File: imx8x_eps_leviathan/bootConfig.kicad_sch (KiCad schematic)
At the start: 24 parts, among them SW1 SW_DIP_x01, U18 BD2204GUL-E2

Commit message: Did stufffffff
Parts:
- C58, C59, C60: footprint (none) -> EPS:C0402
- R100, R101, R84, R85, R86, R87, R88, R89, R90, R91, R92, R93, R94, R95, R96, R97, R98, R99: footprint (none) -> EPS:R0402
- SW1: footprint (none) -> imx8_carrier_board_footprints:SW-SMD_1.27-1P-TPPT
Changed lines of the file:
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@@
 			)
 		)
-		(property "Footprint" ""
+		(property "Footprint" "EPS:R0402"
 			(at 157.226 41.656 90)
 			(effects
@@
 			)
 		)
-		(property "Footprint" ""
+		(property "Footprint" "EPS:C0402"
 			(at 201.6252 33.02 0)
 			(effects
@@
 			)
 		)
-		(property "Footprint" ""
+		(property "Footprint" "EPS:R0402"
 			(at 131.064 28.956 90)
 			(effects
@@
 			)
 		)
-		(property "Footprint" ""
+		(property "Footprint" "EPS:C0402"
 			(at 194.6148 33.02 0)
 			(effects
@@
 			)
 		)
-		(property "Footprint" ""
+		(property "Footprint" "EPS:R0402"
 			(at 30.734 70.866 90)
 			(effects
@@
 			)
 		)
-		(property "Footprint" ""
+		(property "Footprint" "EPS:R0402"
 			(at 152.146 28.956 90)
 			(effects
@@
 			)
 		)
-		(property "Footprint" ""
+		(property "Footprint" "EPS:R0402"
 			(at 115.824 28.956 90)
 			(effects
@@
 			)
 		)
-		(property "Footprint" ""
+		(property "Footprint" "EPS:R0402"
 			(at 43.434 70.866 90)
 			(effects
@@
 			)
 		)
-		(property "Footprint" ""
+		(property "Footprint" "imx8_carrier_board_footprints:SW-SMD_1.27-1P-TPPT"
 			(at 31.75 85.09 0)
 			(effects
@@
 			)
 		)
-		(property "Footprint" ""
+		(property "Footprint" "EPS:R0402"
 			(at 157.226 39.116 90)
 			(effects
@@
 			)
 		)
-		(property "Footprint" ""
+		(property "Footprint" "EPS:R0402"
 			(at 201.676 25.146 90)
 			(effects
@@
 			)
 		)
-		(property "Footprint" ""
+		(property "Footprint" "EPS:R0402"
 			(at 30.734 97.536 90)
 			(effects
@@
 			)
 		)
-		(property "Footprint" ""
+		(property "Footprint" "EPS:R0402"
 			(at 146.304 28.956 90)
 			(effects
@@
 			)
 		)
-		(property "Footprint" ""
+		(property "Footprint" "EPS:R0402"
 			(at 123.444 28.956 90)
 			(effects
@@
 			)
 		)
-		(property "Footprint" ""
+		(property "Footprint" "EPS:R0402"
 			(at 157.226 54.356 90)
 			(effects
@@
 			)
 		)
-		(property "Footprint" ""
+		(property "Footprint" "EPS:C0402"
 			(at 35.56 45.4152 0)
 			(effects
@@
 			)
 		)
-		(property "Footprint" ""
+		(property "Footprint" "EPS:R0402"
 			(at 185.674 26.416 90)
 			(effects
@@
 			)
 		)
-		(property "Footprint" ""
+		(property "Footprint" "EPS:R0402"
 			(at 157.226 36.576 90)
 			(effects
@@
 			)
 		)
-		(property "Footprint" ""
+		(property "Footprint" "EPS:R0402"
 			(at 43.434 97.536 90)
 			(effects
@@
 			)
 		)
-		(property "Footprint" ""
+		(property "Footprint" "EPS:R0402"
 			(at 157.226 51.816 90)
 			(effects
@@
 			)
 		)
-		(property "Footprint" ""
+		(property "Footprint" "EPS:R0402"
 			(at 138.684 28.956 90)
 			(effects
@@
 			)
 		)
-		(property "Footprint" ""
+		(property "Footprint" "EPS:R0402"
 			(at 37.084 97.536 90)
 			(effects

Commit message: bruh
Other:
- title: (none) -> Leviathan 1-A
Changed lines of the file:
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@@
 	(paper "A4")
 	(title_block
+		(title "Leviathan 1-A")
+		(date "2025-10-22")
+		(rev "1-A")
 		(company "Bronco Space Lab")
 		(comment 1 "By John Pollak & Luca Lanzillotta")

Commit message: Updated Schematic and SOM
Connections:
- net VCC_3V3_OUT is gone; now on net +3.3V_OBC: C58.2, U18.A1 (VIN1)
- net VCC_3V3 renamed +3.3V_OBC
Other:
- moved on the sheet: C58, U18

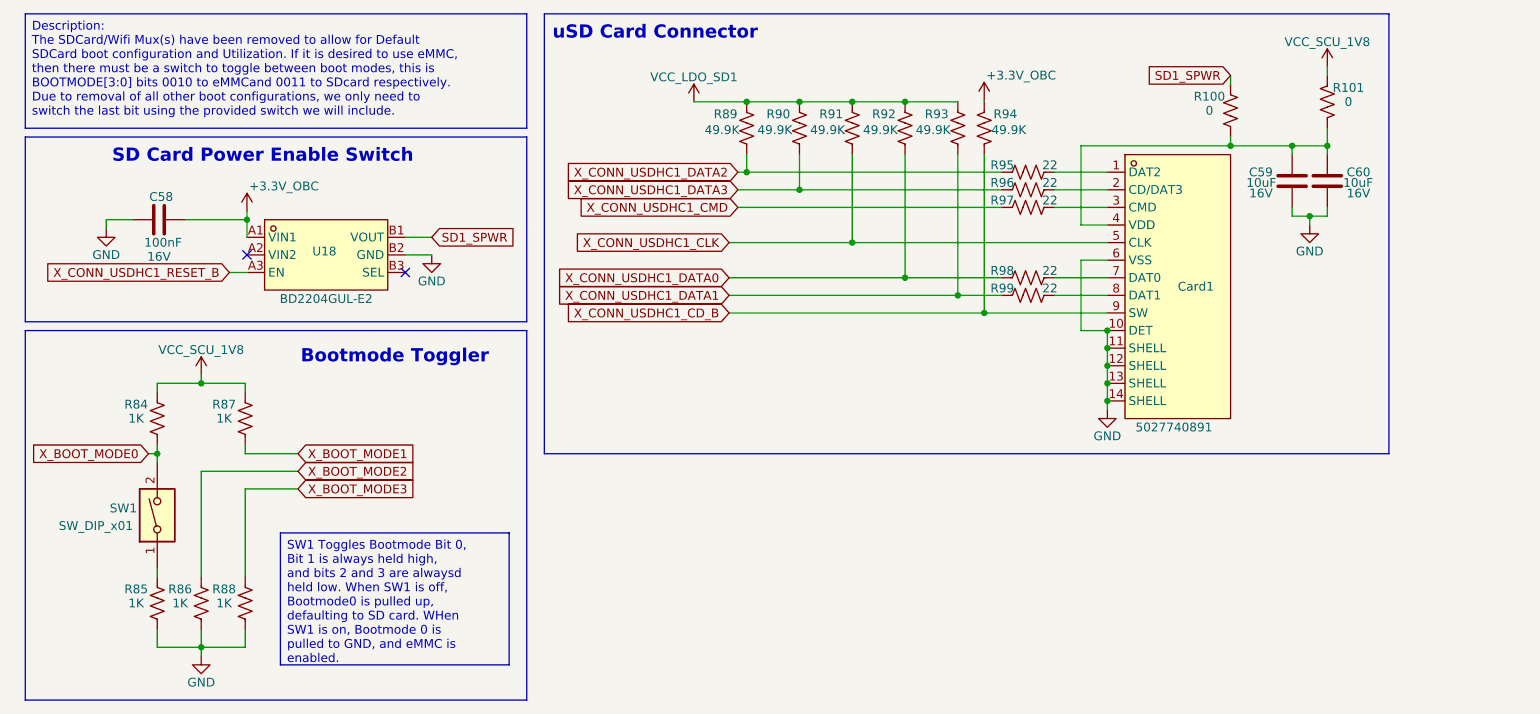
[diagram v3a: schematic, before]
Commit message: Completed Schematic, Started Layout
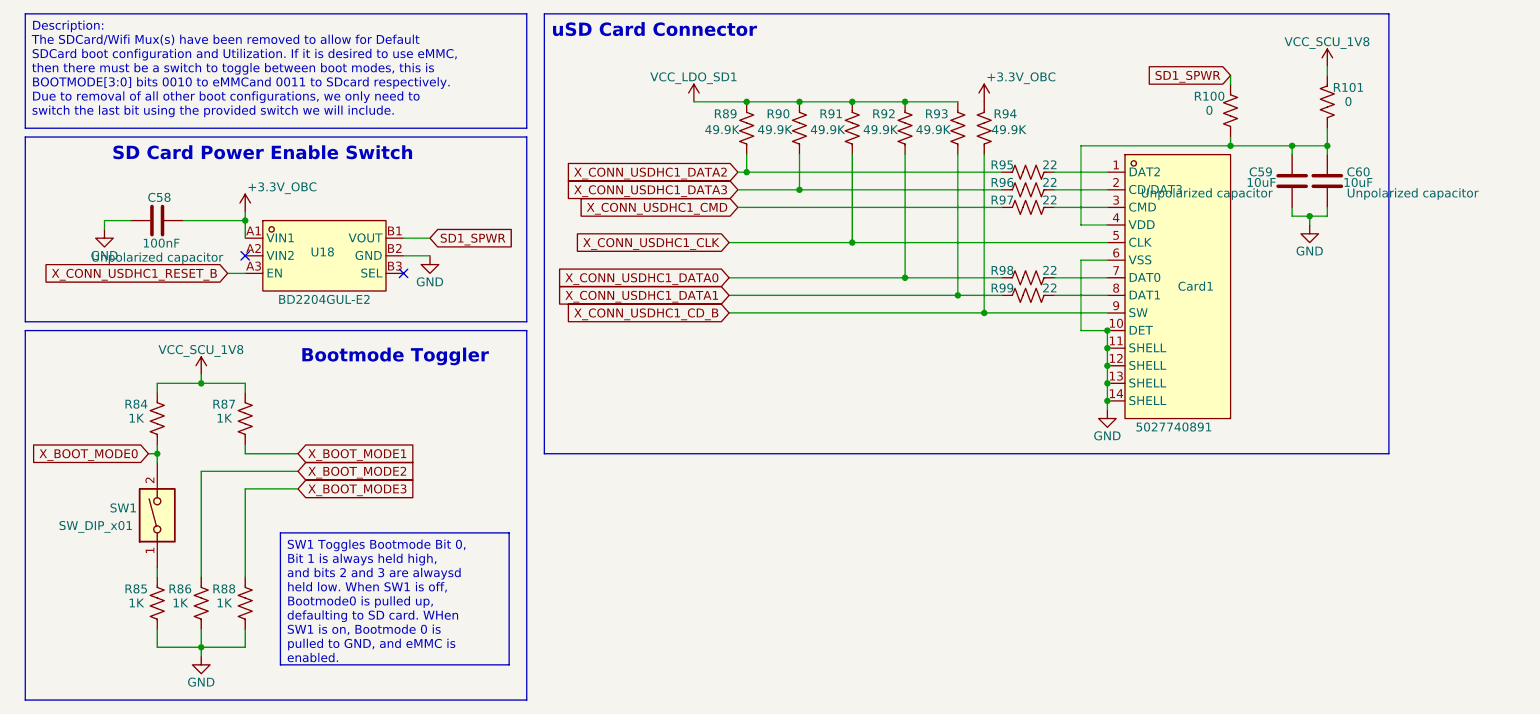
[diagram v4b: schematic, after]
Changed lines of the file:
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@@
 	(title_block
 		(title "Leviathan 1-A")
-		(date "2025-10-22")
+		(date "2025-10-29")
 		(rev "1-A")
 		(company "Bronco Space Lab")
-		(comment 1 "By John Pollak & Luca Lanzillotta")
+		(comment 1 "By Luca Lanzillotta & John Pollack")
 	)
 	(rectangle
@@
 	(text "uSD Card Connector"
 		(exclude_from_sim no)
-		(at 103.632 15.494 0)
+		(at 103.505 15.24 0)
 		(effects
 			(font
@@
 	(text "SD Card Power Enable Switch"
 		(exclude_from_sim no)
-		(at 46.99 33.274 0)
+		(at 46.99 33.02 0)
 		(effects
 			(font
@@
 	)
 	(junction
-		(at 44.704 42.418)
+		(at 44.45 42.545)
 		(diameter 0)
 		(color 0 0 0 0)
@@
 	)
 	(no_connect
-		(at 44.704 47.498)
+		(at 44.45 47.625)
 	)
 	(no_connect
-		(at 67.564 50.038)
+		(at 67.31 50.165)
 	)
 	(wire
@@
 	(wire
 		(pts
-			(xy 67.564 47.498) (xy 71.374 47.498)
+			(xy 67.31 47.625) (xy 71.12 47.625)
 		)
 		(stroke
@@
 	(wire
 		(pts
-			(xy 42.164 50.038) (xy 44.704 50.038)
+			(xy 41.91 50.165) (xy 44.45 50.165)
 		)
 		(stroke
@@
 	(wire
 		(pts
-			(xy 35.814 42.418) (xy 44.704 42.418)
+			(xy 35.56 42.545) (xy 44.45 42.545)
 		)
 		(stroke
@@
 	(wire
 		(pts
-			(xy 24.384 42.418) (xy 24.384 43.688)
+			(xy 24.13 42.545) (xy 24.13 43.815)
 		)
 		(stroke
@@
 	(wire
 		(pts
-			(xy 67.564 44.958) (xy 71.374 44.958)
+			(xy 67.31 45.085) (xy 71.12 45.085)
 		)
 		(stroke
@@
 	(wire
 		(pts
-			(xy 151.13 25.146) (xy 151.13 25.4)
-		)
-		(stroke
-			(width 0)
-			(type default)
-		)
-	)
-	(wire
-		(pts
 			(xy 168.91 58.42) (xy 168.91 60.96)
 		)
@@
 	(wire
 		(pts
-			(xy 28.194 42.418) (xy 24.384 42.418)
+			(xy 27.94 42.545) (xy 24.13 42.545)
 		)
 		(stroke
@@
 	(wire
 		(pts
-			(xy 44.704 42.418) (xy 44.704 41.148)
+			(xy 44.45 42.545) (xy 44.45 41.275)
 		)
 		(stroke
@@
 	(wire
 		(pts
-			(xy 44.704 42.418) (xy 44.704 44.958)
+			(xy 44.45 42.545) (xy 44.45 45.085)
 		)
 		(stroke
@@
 	(global_label "X_CONN_USDHC1_RESET_B"
 		(shape input)
-		(at 42.164 50.038 180)
+		(at 41.91 50.165 180)
 		(fields_autoplaced yes)
 		(effects
@@
 		)
 		(property "Intersheetrefs" "${INTERSHEET_REFS}"
-			(at 14.2023 50.038 0)
+			(at 13.9483 50.165 0)
 			(effects
 				(font
@@
 	(global_label "SD1_SPWR"
 		(shape input)
-		(at 71.374 44.958 0)
+		(at 71.12 45.085 0)
 		(fields_autoplaced yes)
 		(effects
@@
 		)
 		(property "Intersheetrefs" "${INTERSHEET_REFS}"
-			(at 84.2167 44.958 0)
+			(at 83.9627 45.085 0)
 			(effects
 				(font
@@
 			)
 		)
-		(property "Description" "Power symbol creates a global label with name \"VCC_SCU_1V8\""
+		(property "Description" "Power symbol creates a global label with name \"Vdrive\""
 			(at 38.1 64.77 0)
 			(effects
@@
 	(symbol
 		(lib_id "power:GND")
-		(at 24.384 43.688 0)
+		(at 24.13 43.815 0)
 		(unit 1)
 		(exclude_from_sim no)
@@
 		(dnp no)
 		(property "Reference" "#PWR054"
-			(at 24.384 50.038 0)
+			(at 24.13 50.165 0)
 			(effects
 				(font
@@
 		)
 		(property "Value" "GND"
-			(at 24.384 47.498 0)
+			(at 24.13 47.625 0)
 			(effects
 				(font
@@
 		)
 		(property "Footprint" ""
-			(at 24.384 43.688 0)
+			(at 24.13 43.815 0)
 			(effects
 				(font
@@
 		)
 		(property "Datasheet" ""
-			(at 24.384 43.688 0)
+			(at 24.13 43.815 0)
 			(effects
 				(font
@@
 		)
 		(property "Description" "Power symbol creates a global label with name \"GND\" , ground"
-			(at 24.384 43.688 0)
+			(at 24.13 43.815 0)
 			(effects
 				(font
@@
 	(symbol
 		(lib_id "power:GND")
-		(at 71.374 47.498 0)
+		(at 71.12 47.625 0)
 		(unit 1)
 		(exclude_from_sim no)
@@
 		(dnp no)
 		(property "Reference" "#PWR058"
-			(at 71.374 53.848 0)
+			(at 71.12 53.975 0)
 			(effects
 				(font
@@
 		)
 		(property "Value" "GND"
-			(at 71.374 51.308 0)
+			(at 71.12 51.435 0)
 			(effects
 				(font
@@
 		)
 		(property "Footprint" ""
-			(at 71.374 47.498 0)
+			(at 71.12 47.625 0)
 			(effects
 				(font
@@
 		)
 		(property "Datasheet" ""
-			(at 71.374 47.498 0)
+			(at 71.12 47.625 0)
 			(effects
 				(font
@@
 		)
 		(property "Description" "Power symbol creates a global label with name \"GND\" , ground"
-			(at 71.374 47.498 0)
+			(at 71.12 47.625 0)
 			(effects
 				(font
@@
 			)
 		)
-		(property "Description" "Power symbol creates a global label with name \"VCC_SCU_1V8\""
+		(property "Description" "Power symbol creates a global label with name \"Vdrive\""
 			(at 200.66 20.32 0)
 			(effects
@@
 			)
 		)
-		(property "Description" "16V"
+		(property "Description" "Unpolarized capacitor"
 			(at 203.454 38.608 0)
 			(effects
@@
 			)
 		)
-		(property "Description" "Power symbol creates a global label with name \"VCC_LDO_SD1\""
+		(property "Description" "Power symbol creates a global label with name \"VDC\""
 			(at 109.22 25.4 0)
 			(effects
@@
 			)
 		)
-		(property "Description" "16V"
+		(property "Description" "Unpolarized capacitor"
 			(at 192.786 38.608 0)
 			(effects
@@
 	(symbol
 		(lib_id "imx8_carrier_board_symbol_library:BD2204GUL-E2")
-		(at 56.134 47.498 0)
+		(at 55.88 47.625 0)
 		(unit 1)
 		(exclude_from_sim no)
@@
 		(dnp no)
 		(property "Reference" "U18"
-			(at 55.88 46.99 0)
+			(at 55.626 47.117 0)
 			(effects
 				(font
@@
 		)
 		(property "Value" "BD2204GUL-E2"
-			(at 56.134 53.848 0)
+			(at 55.88 53.975 0)
 			(effects
 				(font
@@
 		)
 		(property "Footprint" "imx8_carrier_board_footprints:BGA-6_L1.5-W1.0-P0.50_BD2204GUL-E2"
-			(at 56.134 57.658 0)
+			(at 55.88 57.785 0)
 			(effects
 				(font
@@
 		)
 		(property "Datasheet" "https://lcsc.com/product-detail/Power-Distribution-Switches_ROHM-Semicon-BD2204GUL-E2_C314699.html?s_z=n_BD2204GUL-E2"
-			(at 56.134 47.498 0)
+			(at 55.88 47.625 0)
 			(effects
 				(font
@@
 		)
 		(property "Description" ""
-			(at 56.134 47.498 0)
+			(at 55.88 47.625 0)
 			(effects
 				(font
@@
 		)
 		(property "LCSC Part" "C314699"
-			(at 56.134 60.198 0)
+			(at 55.88 60.325 0)
 			(effects
 				(font
@@
 	(symbol
 		(lib_id "power:+3.3V")
-		(at 151.13 25.146 0)
+		(at 151.13 25.4 0)
 		(unit 1)
 		(exclude_from_sim no)
@@
 		(dnp no)
 		(property "Reference" "#PWR060"
-			(at 151.13 28.956 0)
+			(at 151.13 29.21 0)
 			(effects
 				(font
@@
 		)
 		(property "Value" "+3.3V_OBC"
-			(at 156.464 21.59 0)
+			(at 156.464 21.844 0)
 			(effects
 				(font
@@
 		)
 		(property "Footprint" ""
-			(at 151.13 25.146 0)
+			(at 151.13 25.4 0)
 			(effects
 				(font
@@
 		)
 		(property "Datasheet" ""
-			(at 151.13 25.146 0)
+			(at 151.13 25.4 0)
 			(effects
 				(font
@@
 		)
 		(property "Description" "Power symbol creates a global label with name \"+3.3V\""
-			(at 151.13 25.146 0)
+			(at 151.13 25.4 0)
 			(effects
 				(font
@@
 	(symbol
 		(lib_id "Device:C")
-		(at 32.004 42.418 90)
+		(at 31.75 42.545 90)
 		(mirror x)
 		(unit 1)
@@
 		(dnp no)
 		(property "Reference" "C58"
-			(at 34.036 39.116 90)
+			(at 33.782 39.243 90)
 			(effects
 				(font
@@
 		)
 		(property "Value" "100nF"
-			(at 35.306 45.72 90)
+			(at 35.052 45.847 90)
 			(effects
 				(font
@@
 		)
 		(property "Footprint" "EPS:C0402"
-			(at 35.814 43.3832 0)
+			(at 35.56 43.5102 0)
 			(effects
 				(font
@@
 		)
 		(property "Datasheet" "~"
-			(at 32.004 42.418 0)
+			(at 31.75 42.545 0)
 			(effects
 				(font
@@
 			)
 		)
-		(property "Description" "16V"
-			(at 32.004 47.752 90)
+		(property "Description" "Unpolarized capacitor"
+			(at 31.75 47.879 90)
 			(effects
 				(font
@@
 	(symbol
 		(lib_id "power:+3.3V")
-		(at 44.704 41.148 0)
+		(at 44.45 41.275 0)
 		(unit 1)
 		(exclude_from_sim no)
@@
 		(dnp no)
 		(property "Reference" "#PWR057"
-			(at 44.704 44.958 0)
+			(at 44.45 45.085 0)
 			(effects
 				(font
@@
 		)
 		(property "Value" "+3.3V_OBC"
-			(at 50.038 37.592 0)
+			(at 49.784 37.719 0)
 			(effects
 				(font
@@
 		)
 		(property "Footprint" ""
-			(at 44.704 41.148 0)
+			(at 44.45 41.275 0)
 			(effects
 				(font
@@
 		)
 		(property "Datasheet" ""
-			(at 44.704 41.148 0)
+			(at 44.45 41.275 0)
 			(effects
 				(font
@@
 		)
 		(property "Description" "Power symbol creates a global label with name \"+3.3V\""
-			(at 44.704 41.148 0)
+			(at 44.45 41.275 0)
 			(effects
 				(font

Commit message: Fixed the changes from Phytec
Fixed the issues from the most recent phytec review. Need to still go through the older fixes before the board was merged. This is currently up to date for the what I think is the minimum configuration and use ability.

Thing to note is that there is still a few different sheets that I think need to be added but the major functinallity is there.
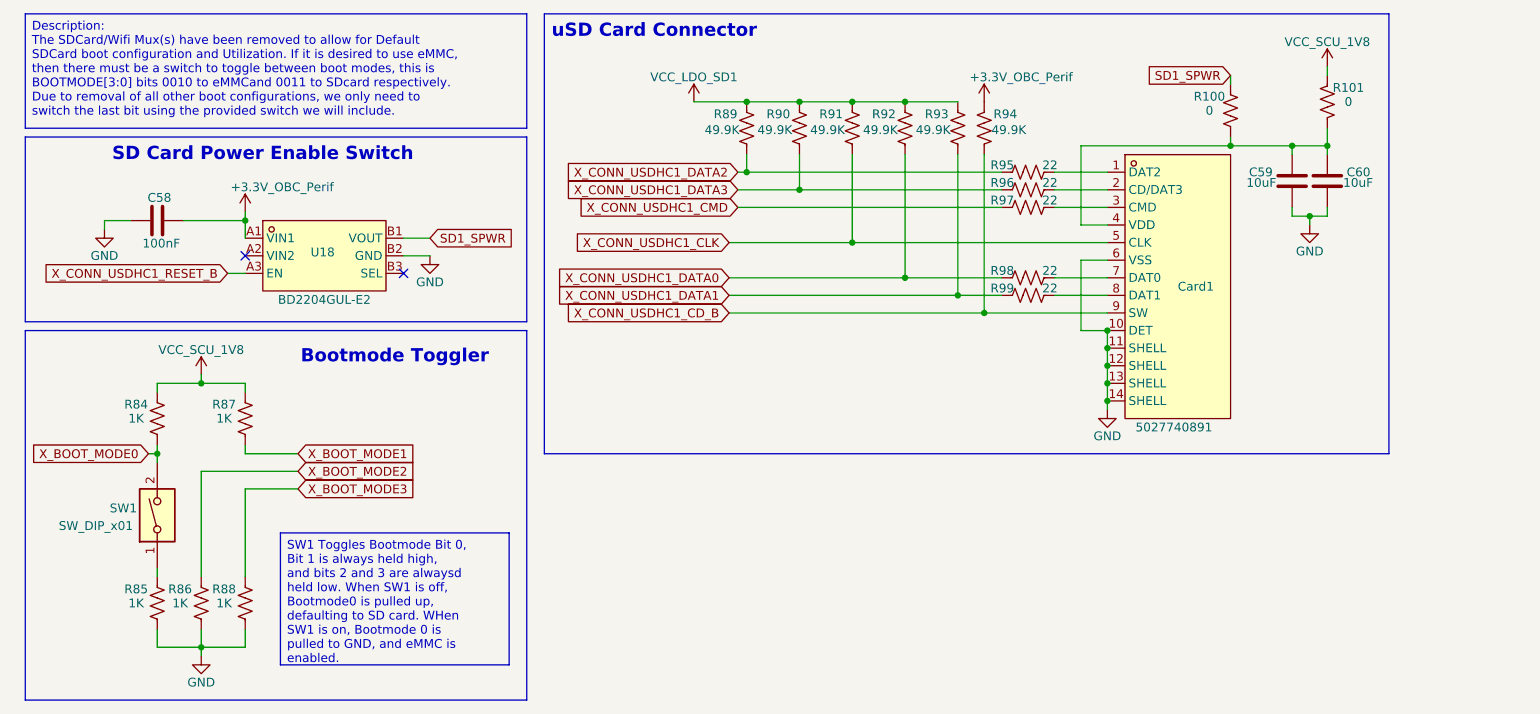
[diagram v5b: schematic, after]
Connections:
- net +3.3V_OBC renamed +3.3V_OBC_Perif
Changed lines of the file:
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@@
 				)
 				(justify left)
+				(hide yes)
 			)
 		)
@@
 				)
 				(justify left)
+				(hide yes)
 			)
 		)
@@
 			)
 		)
-		(property "Value" "+3.3V_OBC"
+		(property "Value" "+3.3V_OBC_Perif"
 			(at 156.464 21.844 0)
 			(effects
@@
 					(size 1.27 1.27)
 				)
+				(hide yes)
 			)
 		)
@@
 			)
 		)
-		(property "Value" "+3.3V_OBC"
+		(property "Value" "+3.3V_OBC_Perif"
 			(at 49.784 37.719 0)
 			(effects
